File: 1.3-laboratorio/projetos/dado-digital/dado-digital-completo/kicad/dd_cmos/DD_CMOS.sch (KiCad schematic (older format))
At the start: 49 parts, among them J1 Conn_01x02, J2 Conn_01x02, J3 Conn_01x01, J4 Conn_01x01, J5 Conn_01x02, Q1 BC547, SW1 SW_PUSH, U1 4093, U2 4027, U3 4518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

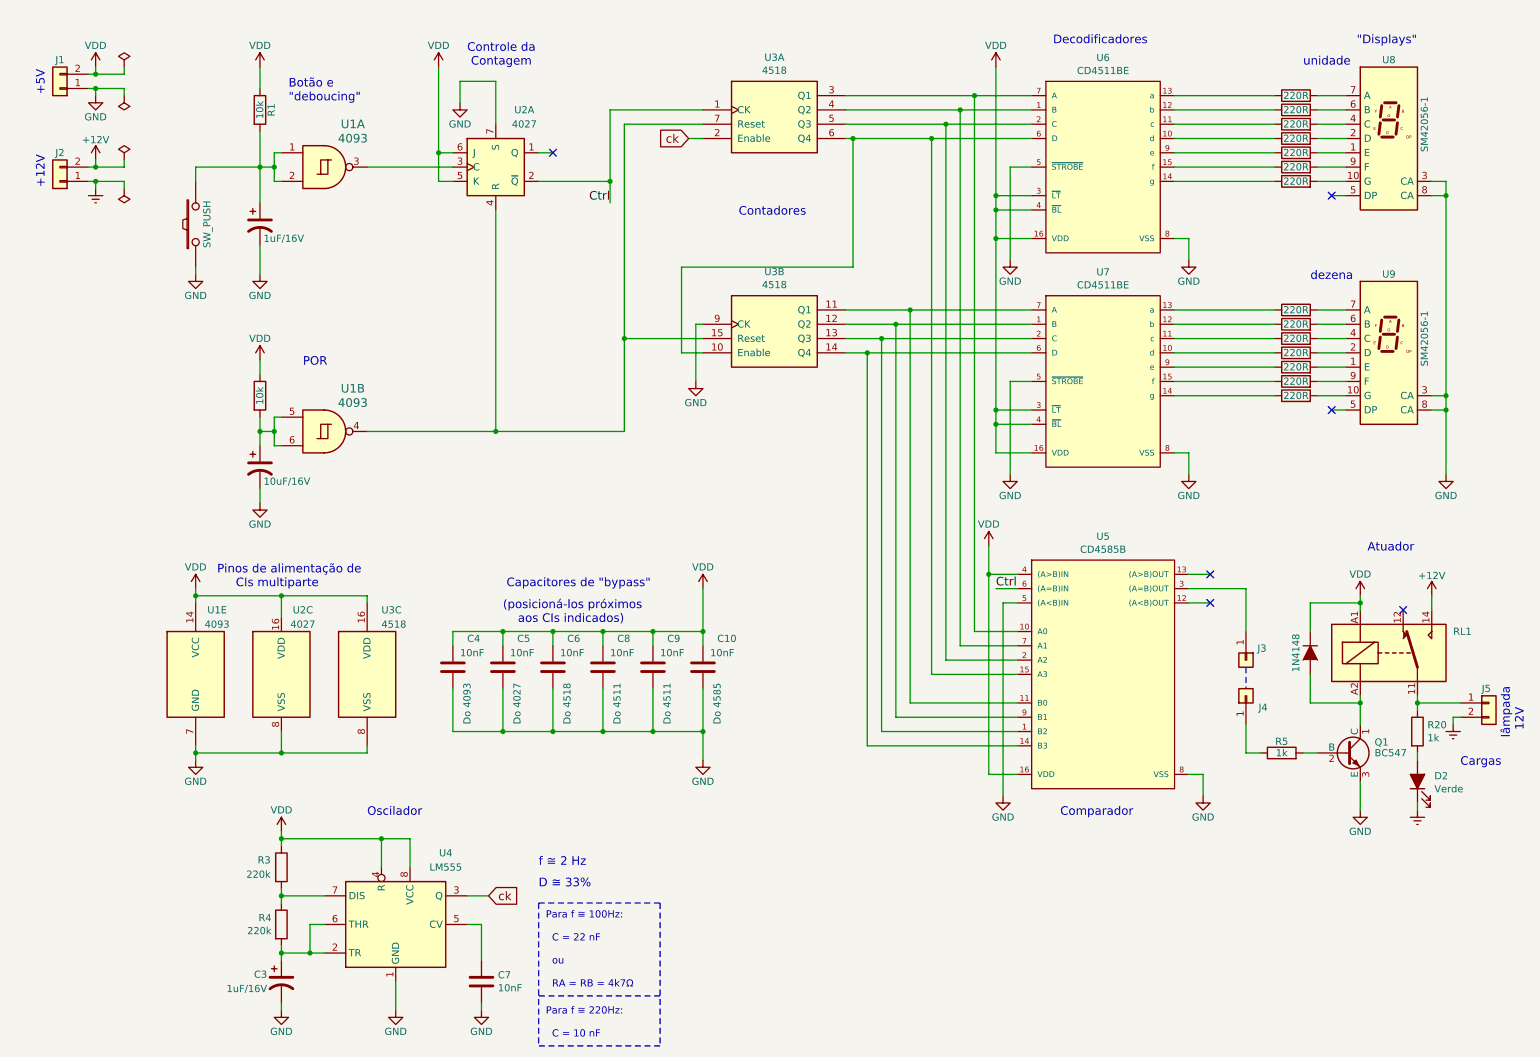
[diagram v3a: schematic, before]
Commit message: Substituição do CD4585 pelo CD74HCT85. Preparação da lista de materiais separada para cada fornecedor.
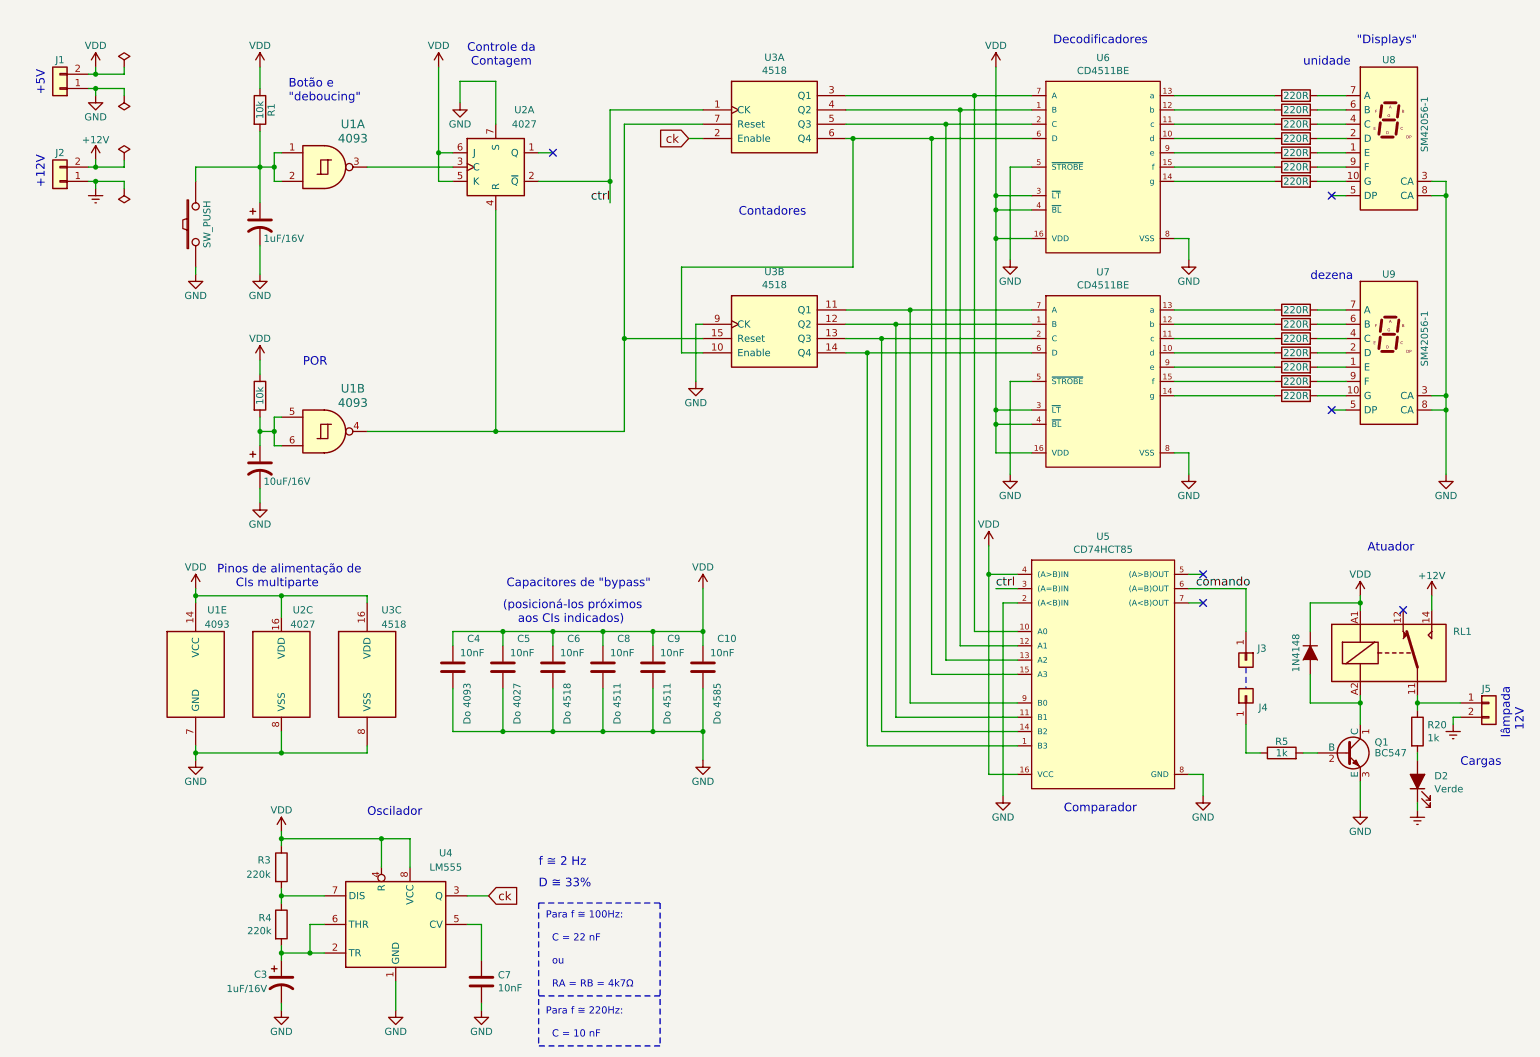
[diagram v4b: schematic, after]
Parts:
- removed U5: CD4585B, Package_DIP:DIP-16_W7.62mm_LongPads, symbol eec:CD4585B
- added U5: CD74HCT85, Package_DIP:DIP-16_W7.62mm_LongPads, symbol eec:CD74HCT85
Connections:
- net GND: now also U5.2 ((A<B)IN), U5.8 (GND)
- net VDD: now also U5.16 (VCC), U5.4 ((A>B)IN)
- net at U3.3 (Q1), U6.7 (A): now also U5.10 (A0)
- net at U3.4 (Q2), U6.1 (B): now also U5.12 (A1)
- net at U3.5 (Q3), U6.2 (C): now also U5.13 (A2)
- net at U3.10 (Enable), U3.6 (Q4), U6.6 (D): now also U5.15 (A3)
- net at U3.11 (Q1), U7.7 (A): now also U5.9 (B0)
- net at U3.12 (Q2), U7.1 (B): now also U5.11 (B1)
- net at U3.13 (Q3), U7.2 (C): now also U5.14 (B2)
- net at U3.14 (Q4), U7.6 (D): now also U5.1 (B3)
- net comando: now reaches J3.1 (Pin_1)
- net comando: now also U5.6 ((A=B)OUT)
- net Ctrl renamed ctrl
- net ctrl: now also U5.3 ((A=B)IN)
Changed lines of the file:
@@
 Sheet 1 1
 Title "Dado Digital - CMOS"
-Date "2022-02-05"
+Date "2022-02-06"
 Rev "1.0"
 Comp "ETE102 - Fundamentos de Circuitos Digitais"
@@
 Connection ~ 1050 1000
 NoConn ~ 9700 3250
-NoConn ~ 8850 4400
-NoConn ~ 8850 4600
+NoConn ~ 8800 4400
+NoConn ~ 8800 4600
 $Comp
 L power:GND #PWR026
@@
 Wire Wire Line
 	8700 3550 8700 3700
-$Comp
-L eec:CD4585B U5
-U 1 1 6220AFA5
-P 7400 4400
-F 0 "U5" H 8100 4665 50  0000 C CNN
-F 1 "CD4585B" H 8100 4574 50  0000 C CNN
-F 2 "Package_DIP:DIP-16_W7.62mm_LongPads" H 7400 4800 50  0001 L CNN
-F 3 "" H 7400 4900 50  0001 L CNN
-F 4 "4" H 7400 5000 50  0001 L CNN "Bits"
-F 5 "SCHS091B" H 7400 5100 50  0001 L CNN "Datasheet Version"
-F 6 "8" H 7400 5200 50  0001 L CNN "F  Nom VoltageMaxMhz"
-F 7 "0.3" H 7400 5300 50  0001 L CNN "ICC  Nom VoltageMaxmA"
-F 8 "CMOS" H 7400 5400 50  0001 L CNN "Input Type"
-F 9 "-55 to 125" H 7400 5500 50  0001 L CNN "Operating Temperature RangeC"
-F 10 "4/-4" H 7400 5600 50  0001 L CNN "Output Drive IOLIOHMaxmA"
-F 11 "CMOS" H 7400 5700 50  0001 L CNN "Output Type"
-F 12 "Military" H 7400 5800 50  0001 L CNN "Rating"
-F 13 "CD4000" H 7400 5900 50  0001 L CNN "Technology Family"
-F 14 "18" H 7400 6000 50  0001 L CNN "VCC Max V"
-F 15 "3" H 7400 6100 50  0001 L CNN "VCC Min V"
-F 16 "10" H 7400 6200 50  0001 L CNN "Voltage Nom V"
-F 17 "IC" H 7400 6300 50  0001 L CNN "category"
-F 18 "19299328" H 7400 6400 50  0001 L CNN "ciiva ids"
-F 19 "97480692d6917754" H 7400 6500 50  0001 L CNN "library id"
-F 20 "Texas Instruments" H 7400 6600 50  0001 L CNN "manufacturer"
-F 21 "N0016A" H 7400 6700 50  0001 L CNN "package"
-F 22 "1459326111" H 7400 6800 50  0001 L CNN "release date"
-F 23 "3DC5686F-0A64-423F-ACFB-3E2A0862EF0D" H 7400 6900 50  0001 L CNN "vault revision"
-F 24 "yes" H 7400 7000 50  0001 L CNN "imported"
-F 25 "250" H 7400 7100 50  0001 L CNN "tpd  Nom VoltageMaxns"
-	1    7400 4400
-	1    0    0    -1
-$EndComp
 Wire Wire Line
 	6450 5600 7500 5600
@@
 	7300 4400 7300 4200
 Wire Wire Line
-	8850 4600 8700 4600
-Wire Wire Line
-	8850 4400 8700 4400
+	8800 4600 8700 4600
+Wire Wire Line
+	8800 4400 8700 4400
 Wire Wire Line
 	8700 4500 9100 4500
@@
 	7500 4500 7350 4500
 Text Label 7350 4500 0    60   ~ 0
-Ctrl
+ctrl
 Text Label 4650 1800 2    60   ~ 0
-Ctrl
+ctrl
 Wire Wire Line
 	4650 1650 4650 1800
@@
 Text Notes 9875 700  0    60   ~ 0
 "Displays"
-Text Notes 7800 6100 0    60   ~ 0
+Text Notes 7825 6075 0    60   ~ 0
 Comparador
 Text Notes 9950 4250 0    60   ~ 0
@@
 $EndComp
 $Comp
-L power:Earth #PWR?
+L power:Earth #PWR032
 U 1 1 62167A6C
 P 10300 6050
-F 0 "#PWR?" H 10300 5800 50  0001 C CNN
+F 0 "#PWR032" H 10300 5800 50  0001 C CNN
 F 1 "Earth" H 10300 5900 50  0001 C CNN
 F 2 "" H 10300 6050 50  0001 C CNN
@@
 	1    0    0    -1
 $EndComp
+$Comp
+L eec:CD74HCT85 U5
+U 1 1 620294E1
+P 7400 4400
+F 0 "U5" H 8100 4665 50  0000 C CNN
+F 1 "CD74HCT85" H 8100 4574 50  0000 C CNN
+F 2 "Package_DIP:DIP-16_W7.62mm_LongPads" H 7400 4800 50  0001 L CNN
+F 3 "" H 7400 4900 50  0001 L CNN
+F 4 "4" H 7400 5000 50  0001 L CNN "Bits"
+F 5 "SCHS136E" H 7400 5100 50  0001 L CNN "Datasheet Version"
+F 6 "70" H 7400 5200 50  0001 L CNN "F  Nom VoltageMaxMhz"
+F 7 "0.08" H 7400 5300 50  0001 L CNN "ICC  Nom VoltageMaxmA"
+F 8 "TTL" H 7400 5400 50  0001 L CNN "Input Type"
+F 9 "-55 to 125" H 7400 5500 50  0001 L CNN "Operating Temperature RangeC"
+F 10 "4/-4" H 7400 5600 50  0001 L CNN "Output Drive IOLIOHMaxmA"
+F 11 "CMOS" H 7400 5700 50  0001 L CNN "Output Type"
+F 12 "Catalog" H 7400 5800 50  0001 L CNN "Rating"
+F 13 "No" H 7400 5900 50  0001 L CNN "Schmitt Trigger"
+F 14 "HCT" H 7400 6000 50  0001 L CNN "Technology Family"
+F 15 "5.5" H 7400 6100 50  0001 L CNN "VCC Max V"
+F 16 "4.5" H 7400 6200 50  0001 L CNN "VCC Min V"
+F 17 "4.5" H 7400 6300 50  0001 L CNN "Voltage Nom V"
+F 18 "IC" H 7400 6400 50  0001 L CNN "category"
+F 19 "1166062" H 7400 6500 50  0001 L CNN "ciiva ids"
+F 20 "fa29bd229b596f21" H 7400 6600 50  0001 L CNN "library id"
+F 21 "Texas Instruments" H 7400 6700 50  0001 L CNN "manufacturer"
+F 22 "D0016A" H 7400 6800 50  0001 L CNN "package"
+F 23 "1459323913" H 7400 6900 50  0001 L CNN "release date"
+F 24 "D5493793-D314-4725-94A2-C5A5787CEF4A" H 7400 7000 50  0001 L CNN "vault revision"
+F 25 "yes" H 7400 7100 50  0001 L CNN "imported"
+F 26 "50" H 7400 7200 50  0001 L CNN "tpd  Nom VoltageMaxns"
+	1    7400 4400
+	1    0    0    -1
+$EndComp
+Text Label 8750 4500 0    60   ~ 0
+comando
 $EndSCHEMATC

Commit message: Concluído o leiaute da PCI do módulo 'Atuador e Carga' do Dado Digital Completo. Falta fazer a revisão final e solicitar o orçamento.
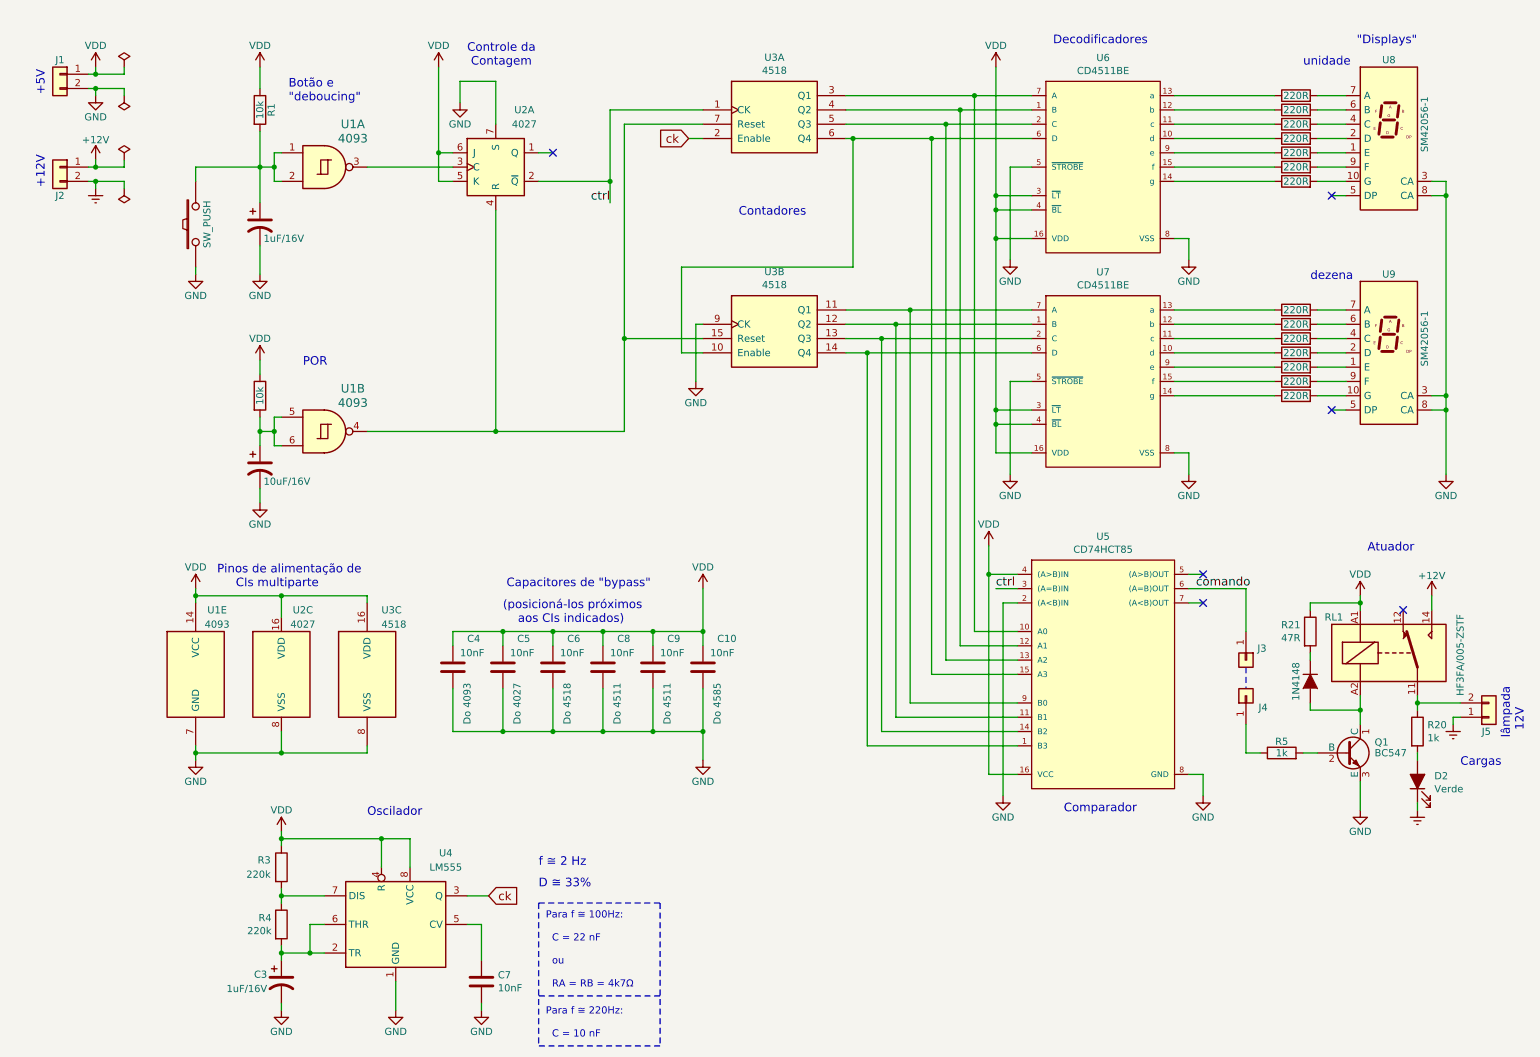
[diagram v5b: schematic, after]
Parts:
- added R21: 47R, Resistor_THT:R_Axial_DIN0207_L6.3mm_D2.5mm_P10.16mm_Horizontal, symbol DD_CMOS-rescue:R
- RL1: value FINDER-40.51 -> HF3FA/005-ZSTF
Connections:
- net +12V: now also J2.1 (Pin_1); no longer J2.2 (Pin_2)
- net Earth: now also J2.2 (Pin_2), J5.1 (Pin_1); no longer J2.1 (Pin_1), J5.2 (Pin_2)
- net GND: now also J1.2 (Pin_2); no longer J1.1 (Pin_1)
- net VDD: now also J1.1 (Pin_1), R21.1; no longer D1.1 (K), J1.2 (Pin_2)
- net at R20.1, RL1.11: now also J5.2 (Pin_2); no longer J5.1 (Pin_1)
- new net: D1.1 (K), R21.2
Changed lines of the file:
@@
 L DD_CMOS-rescue:D D1
 U 1 1 5742CB78
-P 9550 4950
-F 0 "D1" H 9550 5050 50  0001 C CNN
-F 1 "1N4148" H 9550 4850 50  0000 C CNN
-F 2 "Diode_THT:D_DO-34_SOD68_P7.62mm_Horizontal" H 9550 4950 50  0001 C CNN
-F 3 "" H 9550 4950 50  0000 C CNN
-	1    9550 4950
+P 9550 5150
+F 0 "D1" H 9550 5250 50  0001 C CNN
+F 1 "1N4148" H 9550 5050 50  0000 C CNN
+F 2 "Diode_THT:D_DO-34_SOD68_P7.62mm_Horizontal" H 9550 5150 50  0001 C CNN
+F 3 "" H 9550 5150 50  0000 C CNN
+	1    9550 5150
 	0    1    1    0
 $EndComp
@@
 	10500 3250 10500 3700
 Wire Wire Line
-	9900 5250 9900 5300
-Wire Wire Line
-	9900 5300 9900 5450
-Wire Wire Line
-	9550 5300 9900 5300
-Connection ~ 9900 5300
-Wire Wire Line
-	9550 4600 9550 4800
+	9900 5250 9900 5350
+Wire Wire Line
+	9900 5350 9900 5450
+Wire Wire Line
+	9550 5350 9900 5350
+Connection ~ 9900 5350
+Wire Wire Line
+	9550 4600 9550 4650
 Wire Wire Line
 	5300 2650 5250 2650
@@
 	9500 5650 9600 5650
 Wire Wire Line
-	9550 5300 9550 5100
+	9550 5350 9550 5300
 $Comp
 L power:VDD #PWR022
@@
 U 1 1 575012BB
 P 10100 4950
-F 0 "RL1" H 10550 5100 50  0000 L CNN
-F 1 "FINDER-40.51" H 10550 5000 50  0001 L CNN
+F 0 "RL1" H 9650 5200 50  0000 L CNN
+F 1 "HF3FA/005-ZSTF" V 10600 4650 50  0000 L CNN
 F 2 "Relay_THT:Relay_SPDT_SANYOU_SRD_Series_Form_C" H 10100 4950 50  0001 C CNN
 F 3 "" H 10100 4950 50  0000 C CNN
@@
 L Connector_Generic:Conn_01x02 J1
 U 1 1 620818EA
-P 800 1000
-F 0 "J1" H 800 800 50  0000 C CNN
-F 1 "Conn_01x02" H 718 766 50  0001 C CNN
-F 2 "TerminalBlock_Phoenix:TerminalBlock_Phoenix_MKDS-1,5-2_1x02_P5.00mm_Horizontal" H 800 1000 50  0001 C CNN
-F 3 "~" H 800 1000 50  0001 C CNN
-	1    800  1000
-	-1   0    0    1
+P 800 900
+F 0 "J1" H 800 1000 50  0000 C CNN
+F 1 "Conn_01x02" H 718 666 50  0001 C CNN
+F 2 "TerminalBlock_Phoenix:TerminalBlock_Phoenix_MKDS-1,5-2_1x02_P5.00mm_Horizontal" H 800 900 50  0001 C CNN
+F 3 "~" H 800 900 50  0001 C CNN
+	1    800  900
+	-1   0    0    -1
 $EndComp
 $Comp
 L Connector_Generic:Conn_01x02 J2
 U 1 1 620839E4
-P 800 1650
-F 0 "J2" H 800 1450 50  0000 C CNN
-F 1 "Conn_01x02" H 718 1416 50  0001 C CNN
-F 2 "TerminalBlock_Phoenix:TerminalBlock_Phoenix_MKDS-1,5-2_1x02_P5.00mm_Horizontal" H 800 1650 50  0001 C CNN
-F 3 "~" H 800 1650 50  0001 C CNN
-	1    800  1650
-	-1   0    0    1
+P 800 1550
+F 0 "J2" H 800 1350 50  0000 C CNN
+F 1 "Conn_01x02" H 718 1316 50  0001 C CNN
+F 2 "TerminalBlock_Phoenix:TerminalBlock_Phoenix_MKDS-1,5-2_1x02_P5.00mm_Horizontal" H 800 1550 50  0001 C CNN
+F 3 "~" H 800 1550 50  0001 C CNN
+	1    800  1550
+	-1   0    0    -1
 $EndComp
 $Comp
 L Connector_Generic:Conn_01x02 J5
 U 1 1 62084076
-P 10800 5300
-F 0 "J5" H 10750 5400 50  0000 L CNN
-F 1 "Conn_01x02" H 10718 5066 50  0001 C CNN
-F 2 "TerminalBlock_Phoenix:TerminalBlock_Phoenix_MKDS-1,5-2_1x02_P5.00mm_Horizontal" H 10800 5300 50  0001 C CNN
-F 3 "~" H 10800 5300 50  0001 C CNN
-	1    10800 5300
-	1    0    0    -1
+P 10800 5400
+F 0 "J5" H 10750 5500 50  0000 L CNN
+F 1 "Conn_01x02" H 10718 5166 50  0001 C CNN
+F 2 "TerminalBlock_Phoenix:TerminalBlock_Phoenix_MKDS-1,5-2_1x02_P5.00mm_Horizontal" H 10800 5400 50  0001 C CNN
+F 3 "~" H 10800 5400 50  0001 C CNN
+	1    10800 5400
+	1    0    0    1
 $EndComp
 $Comp
@@
 Text Label 8750 4500 0    60   ~ 0
 comando
+$Comp
+L DD_CMOS-rescue:R R21
+U 1 1 6204C159
+P 9550 4800
+F 0 "R21" H 9481 4846 50  0000 R CNN
+F 1 "47R" H 9481 4755 50  0000 R CNN
+F 2 "Resistor_THT:R_Axial_DIN0207_L6.3mm_D2.5mm_P10.16mm_Horizontal" V 9480 4800 50  0001 C CNN
+F 3 "" H 9550 4800 50  0000 C CNN
+	1    9550 4800
+	1    0    0    -1
+$EndComp
+Wire Wire Line
+	9550 4950 9550 5000
 $EndSCHEMATC
